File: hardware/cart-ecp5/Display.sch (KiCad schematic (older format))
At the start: 10 parts

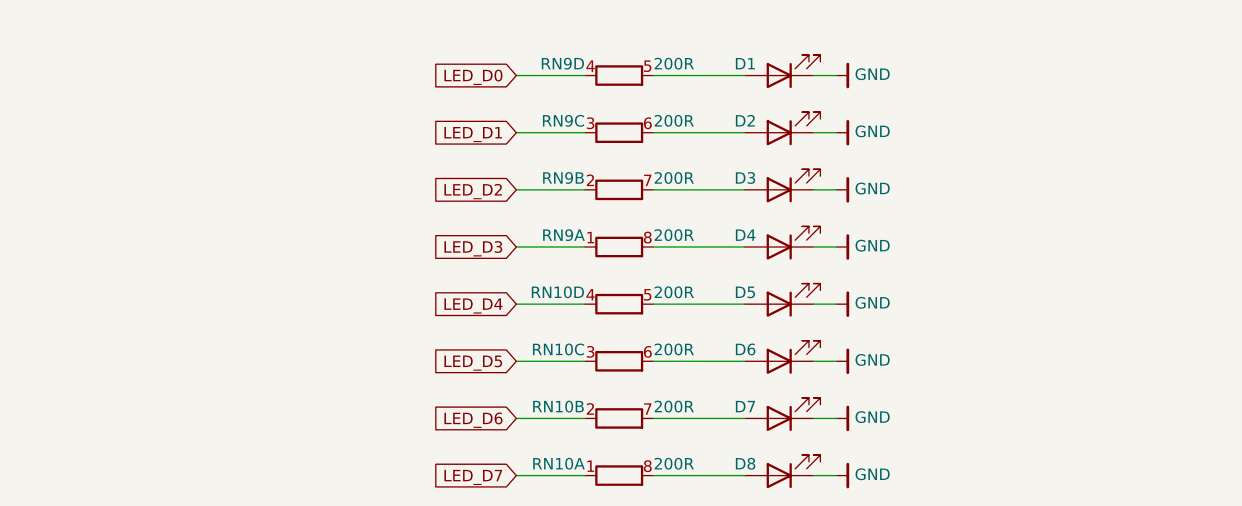
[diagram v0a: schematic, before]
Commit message: Add configuration done LED
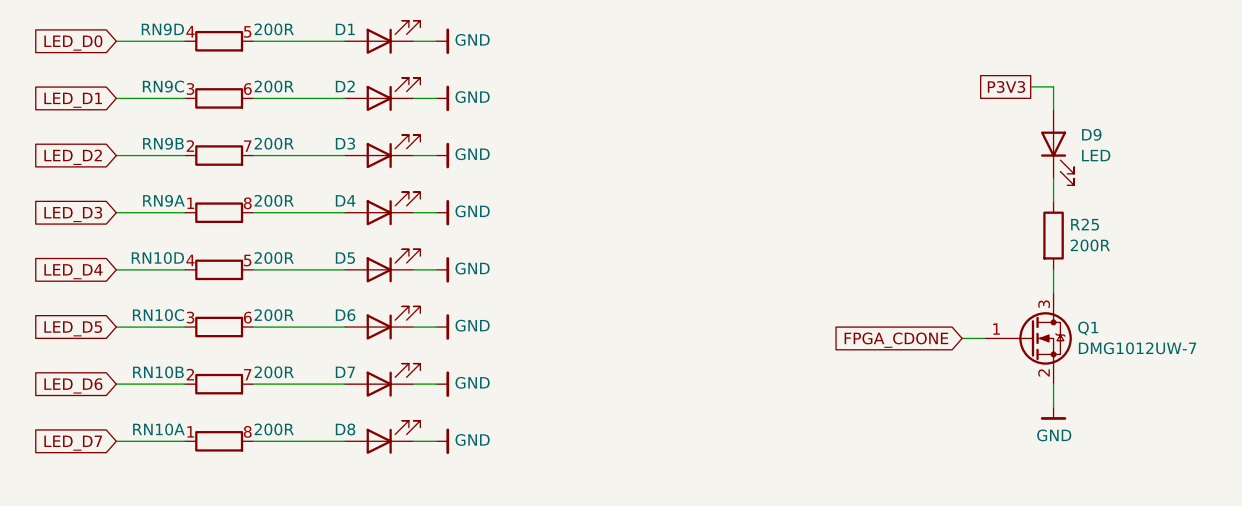
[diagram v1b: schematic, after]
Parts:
- added D9: LED, Diode_SMD:D_0603_1608Metric, symbol Device:LED
- added Q1: DMG1012UW-7, Package_TO_SOT_SMD:SOT-323_SC-70, symbol Device:Q_NMOS_GSD
- added R25: 200R, Resistor_SMD:R_0402_1005Metric, symbol Device:R
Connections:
- net GND: now also Q1.2 (S)
- new net: Q1.3 (D), R25.2
- new net: D9.1 (K), R25.1
- new net FPGA_CDONE: Q1.1 (G)
- new net P3V3: D9.2 (A)
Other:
- moved on the sheet: D1, D2, D3, D4, D5, D6, D7, D8, RN10A, RN10B, RN10C, RN10D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

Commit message: Use LTST-C191KGKT as our 0603 green LED
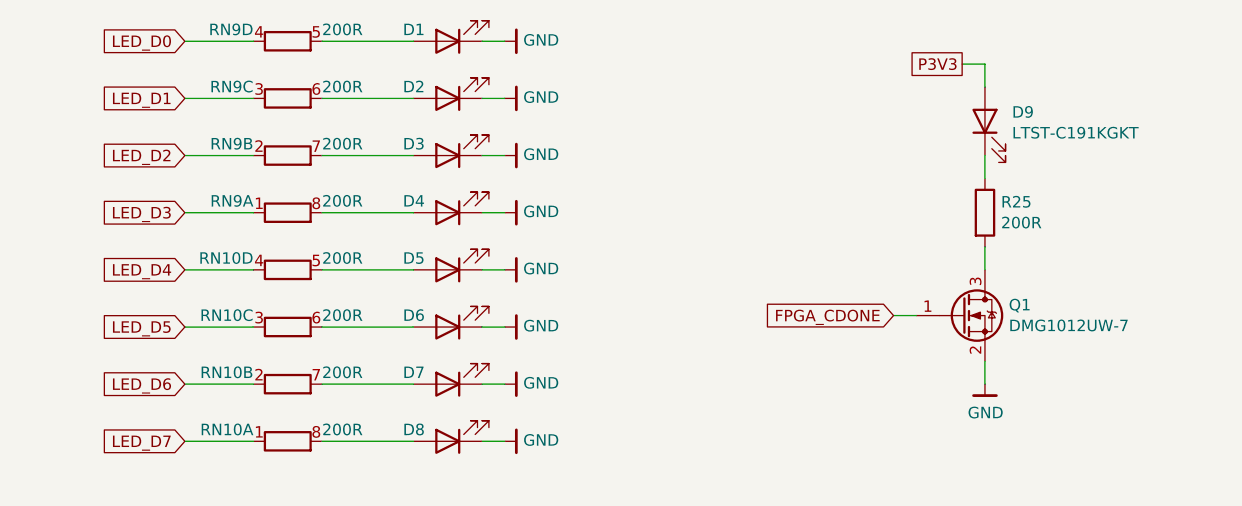
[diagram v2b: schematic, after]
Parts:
- D1, D2, D3, D4, D5, D6, D7, D8, D9: value LED -> LTST-C191KGKT
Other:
- moved on the sheet: D1, D2, D3, D4, D5, D6, D7, D8, D9, Q1, R25, RN10A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

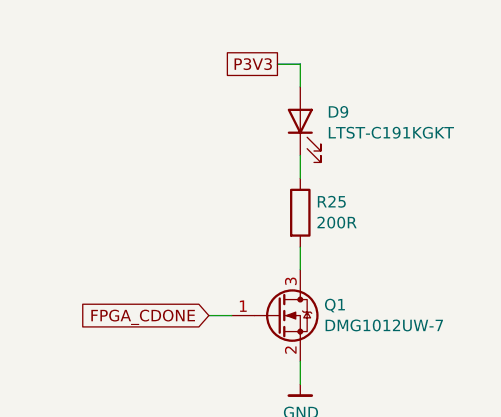
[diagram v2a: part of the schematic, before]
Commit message: Check all resistor values for power management and assign MPN for caps and resistors
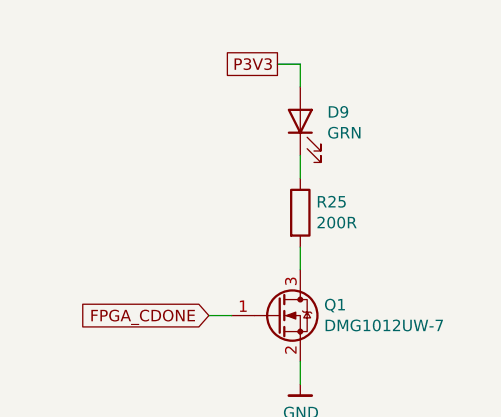
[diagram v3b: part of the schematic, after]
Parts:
- D1, D2, D3, D4, D5, D6, D7, D8, D9: value LTST-C191KGKT -> GRN; MFR (none) -> Lite-On; MPN (none) -> LTST-C191KGKT
- Q1: MFR (none) -> Diodes; MPN (none) -> DMG1012UW-7
- R25: MFR (none) -> Yageo; MPN (none) -> RC0402JR-07200RL
- RN10, RN9: MFR (none) -> Yageo; MPN (none) -> YC164-JR-07200RL
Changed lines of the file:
@@
 P 5150 3050
 F 0 "D1" H 5250 3000 50  0000 L CNN
-F 1 "LTST-C191KGKT" H 5143 3176 50  0001 C CNN
+F 1 "GRN" H 5143 3176 50  0001 C CNN
 F 2 "Diode_SMD:D_0603_1608Metric" H 5150 3050 50  0001 C CNN
 F 3 "~" H 5150 3050 50  0001 C CNN
+F 4 "Lite-On" H 5150 3050 50  0001 C CNN "MFR"
+F 5 "LTST-C191KGKT" H 5150 3050 50  0001 C CNN "MPN"
 	1    5150 3050
 	-1   0    0    1
@@
 F 2 "Resistor_SMD:R_Array_Convex_4x0603" V 4370 3800 50  0001 C CNN
 F 3 "~" H 4450 3800 50  0001 C CNN
+F 4 "Yageo" H 4450 3800 50  0001 C CNN "MFR"
+F 5 "YC164-JR-07200RL" H 4450 3800 50  0001 C CNN "MPN"
 	1    4450 3800
 	0    1    1    0
@@
 P 5150 3300
 F 0 "D2" H 5250 3250 50  0000 L CNN
-F 1 "LTST-C191KGKT" H 5143 3426 50  0001 C CNN
+F 1 "GRN" H 5143 3426 50  0001 C CNN
 F 2 "Diode_SMD:D_0603_1608Metric" H 5150 3300 50  0001 C CNN
 F 3 "~" H 5150 3300 50  0001 C CNN
+F 4 "Lite-On" H 5150 3300 50  0001 C CNN "MFR"
+F 5 "LTST-C191KGKT" H 5150 3300 50  0001 C CNN "MPN"
 	1    5150 3300
 	-1   0    0    1
@@
 F 2 "Resistor_SMD:R_Array_Convex_4x0603" V 4370 3550 50  0001 C CNN
 F 3 "~" H 4450 3550 50  0001 C CNN
+F 4 "Yageo" H 4450 3550 50  0001 C CNN "MFR"
+F 5 "YC164-JR-07200RL" H 4450 3550 50  0001 C CNN "MPN"
 	2    4450 3550
 	0    1    1    0
@@
 P 5150 3550
 F 0 "D3" H 5250 3500 50  0000 L CNN
-F 1 "LTST-C191KGKT" H 5143 3676 50  0001 C CNN
+F 1 "GRN" H 5143 3676 50  0001 C CNN
 F 2 "Diode_SMD:D_0603_1608Metric" H 5150 3550 50  0001 C CNN
 F 3 "~" H 5150 3550 50  0001 C CNN
+F 4 "Lite-On" H 5150 3550 50  0001 C CNN "MFR"
+F 5 "LTST-C191KGKT" H 5150 3550 50  0001 C CNN "MPN"
 	1    5150 3550
 	-1   0    0    1
@@
 F 2 "Resistor_SMD:R_Array_Convex_4x0603" V 4370 3300 50  0001 C CNN
 F 3 "~" H 4450 3300 50  0001 C CNN
+F 4 "Yageo" H 4450 3300 50  0001 C CNN "MFR"
+F 5 "YC164-JR-07200RL" H 4450 3300 50  0001 C CNN "MPN"
 	3    4450 3300
 	0    1    1    0
@@
 P 5150 3800
 F 0 "D4" H 5250 3750 50  0000 L CNN
-F 1 "LTST-C191KGKT" H 5143 3926 50  0001 C CNN
+F 1 "GRN" H 5143 3926 50  0001 C CNN
 F 2 "Diode_SMD:D_0603_1608Metric" H 5150 3800 50  0001 C CNN
 F 3 "~" H 5150 3800 50  0001 C CNN
+F 4 "Lite-On" H 5150 3800 50  0001 C CNN "MFR"
+F 5 "LTST-C191KGKT" H 5150 3800 50  0001 C CNN "MPN"
 	1    5150 3800
 	-1   0    0    1
@@
 F 2 "Resistor_SMD:R_Array_Convex_4x0603" V 4370 3050 50  0001 C CNN
 F 3 "~" H 4450 3050 50  0001 C CNN
+F 4 "Yageo" H 4450 3050 50  0001 C CNN "MFR"
+F 5 "YC164-JR-07200RL" H 4450 3050 50  0001 C CNN "MPN"
 	4    4450 3050
 	0    1    1    0
@@
 P 5150 4050
 F 0 "D5" H 5250 4000 50  0000 L CNN
-F 1 "LTST-C191KGKT" H 5143 4176 50  0001 C CNN
+F 1 "GRN" H 5143 4176 50  0001 C CNN
 F 2 "Diode_SMD:D_0603_1608Metric" H 5150 4050 50  0001 C CNN
 F 3 "~" H 5150 4050 50  0001 C CNN
+F 4 "Lite-On" H 5150 4050 50  0001 C CNN "MFR"
+F 5 "LTST-C191KGKT" H 5150 4050 50  0001 C CNN "MPN"
 	1    5150 4050
 	-1   0    0    1
@@
 F 2 "Resistor_SMD:R_Array_Convex_4x0603" V 4370 4800 50  0001 C CNN
 F 3 "~" H 4450 4800 50  0001 C CNN
+F 4 "Yageo" H 4450 4800 50  0001 C CNN "MFR"
+F 5 "YC164-JR-07200RL" H 4450 4800 50  0001 C CNN "MPN"
 	1    4450 4800
 	0    1    1    0
@@
 P 5150 4300
 F 0 "D6" H 5250 4250 50  0000 L CNN
-F 1 "LTST-C191KGKT" H 5143 4426 50  0001 C CNN
+F 1 "GRN" H 5143 4426 50  0001 C CNN
 F 2 "Diode_SMD:D_0603_1608Metric" H 5150 4300 50  0001 C CNN
 F 3 "~" H 5150 4300 50  0001 C CNN
+F 4 "Lite-On" H 5150 4300 50  0001 C CNN "MFR"
+F 5 "LTST-C191KGKT" H 5150 4300 50  0001 C CNN "MPN"
 	1    5150 4300
 	-1   0    0    1
@@
 F 2 "Resistor_SMD:R_Array_Convex_4x0603" V 4370 4550 50  0001 C CNN
 F 3 "~" H 4450 4550 50  0001 C CNN
+F 4 "Yageo" H 4450 4550 50  0001 C CNN "MFR"
+F 5 "YC164-JR-07200RL" H 4450 4550 50  0001 C CNN "MPN"
 	2    4450 4550
 	0    1    1    0
@@
 P 5150 4550
 F 0 "D7" H 5250 4500 50  0000 L CNN
-F 1 "LTST-C191KGKT" H 5143 4676 50  0001 C CNN
+F 1 "GRN" H 5143 4676 50  0001 C CNN
 F 2 "Diode_SMD:D_0603_1608Metric" H 5150 4550 50  0001 C CNN
 F 3 "~" H 5150 4550 50  0001 C CNN
+F 4 "Lite-On" H 5150 4550 50  0001 C CNN "MFR"
+F 5 "LTST-C191KGKT" H 5150 4550 50  0001 C CNN "MPN"
 	1    5150 4550
 	-1   0    0    1
@@
 F 2 "Resistor_SMD:R_Array_Convex_4x0603" V 4370 4300 50  0001 C CNN
 F 3 "~" H 4450 4300 50  0001 C CNN
+F 4 "Yageo" H 4450 4300 50  0001 C CNN "MFR"
+F 5 "YC164-JR-07200RL" H 4450 4300 50  0001 C CNN "MPN"
 	3    4450 4300
 	0    1    1    0
@@
 P 5150 4800
 F 0 "D8" H 5250 4750 50  0000 L CNN
-F 1 "LTST-C191KGKT" H 5143 4926 50  0001 C CNN
+F 1 "GRN" H 5143 4926 50  0001 C CNN
 F 2 "Diode_SMD:D_0603_1608Metric" H 5150 4800 50  0001 C CNN
 F 3 "~" H 5150 4800 50  0001 C CNN
+F 4 "Lite-On" H 5150 4800 50  0001 C CNN "MFR"
+F 5 "LTST-C191KGKT" H 5150 4800 50  0001 C CNN "MPN"
 	1    5150 4800
 	-1   0    0    1
@@
 F 2 "Resistor_SMD:R_Array_Convex_4x0603" V 4370 4050 50  0001 C CNN
 F 3 "~" H 4450 4050 50  0001 C CNN
+F 4 "Yageo" H 4450 4050 50  0001 C CNN "MFR"
+F 5 "YC164-JR-07200RL" H 4450 4050 50  0001 C CNN "MPN"
 	4    4450 4050
 	0    1    1    0
@@
 F 2 "Package_TO_SOT_SMD:SOT-323_SC-70" H 7600 4350 50  0001 C CNN
 F 3 "https://datasheet.lcsc.com/szlcsc/1811061813_ON-Semiconductor-FDV301N_C15310.pdf" H 7400 4250 50  0001 C CNN
+F 4 "Diodes" H 7400 4250 50  0001 C CNN "MFR"
+F 5 "DMG1012UW-7" H 7400 4250 50  0001 C CNN "MPN"
 	1    7400 4250
 	1    0    0    -1
@@
 F 2 "Resistor_SMD:R_0402_1005Metric" V 7430 3800 50  0001 C CNN
 F 3 "~" H 7500 3800 50  0001 C CNN
+F 4 "RC0402JR-07200RL" H 7500 3800 50  0001 C CNN "MPN"
+F 5 "Yageo" H 7500 3800 50  0001 C CNN "MFR"
 	1    7500 3800
 	1    0    0    -1
@@
 P 7500 3400
 F 0 "D9" V 7539 3282 50  0000 R CNN
-F 1 "LTST-C191KGKT" V 7448 3282 50  0000 R CNN
+F 1 "GRN" V 7448 3282 50  0000 R CNN
 F 2 "Diode_SMD:D_0603_1608Metric" H 7500 3400 50  0001 C CNN
 F 3 "~" H 7500 3400 50  0001 C CNN
+F 4 "Lite-On" H 7500 3400 50  0001 C CNN "MFR"
+F 5 "LTST-C191KGKT" H 7500 3400 50  0001 C CNN "MPN"
 	1    7500 3400
 	0    -1   -1   0
